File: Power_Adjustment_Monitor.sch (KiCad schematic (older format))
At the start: 15 parts

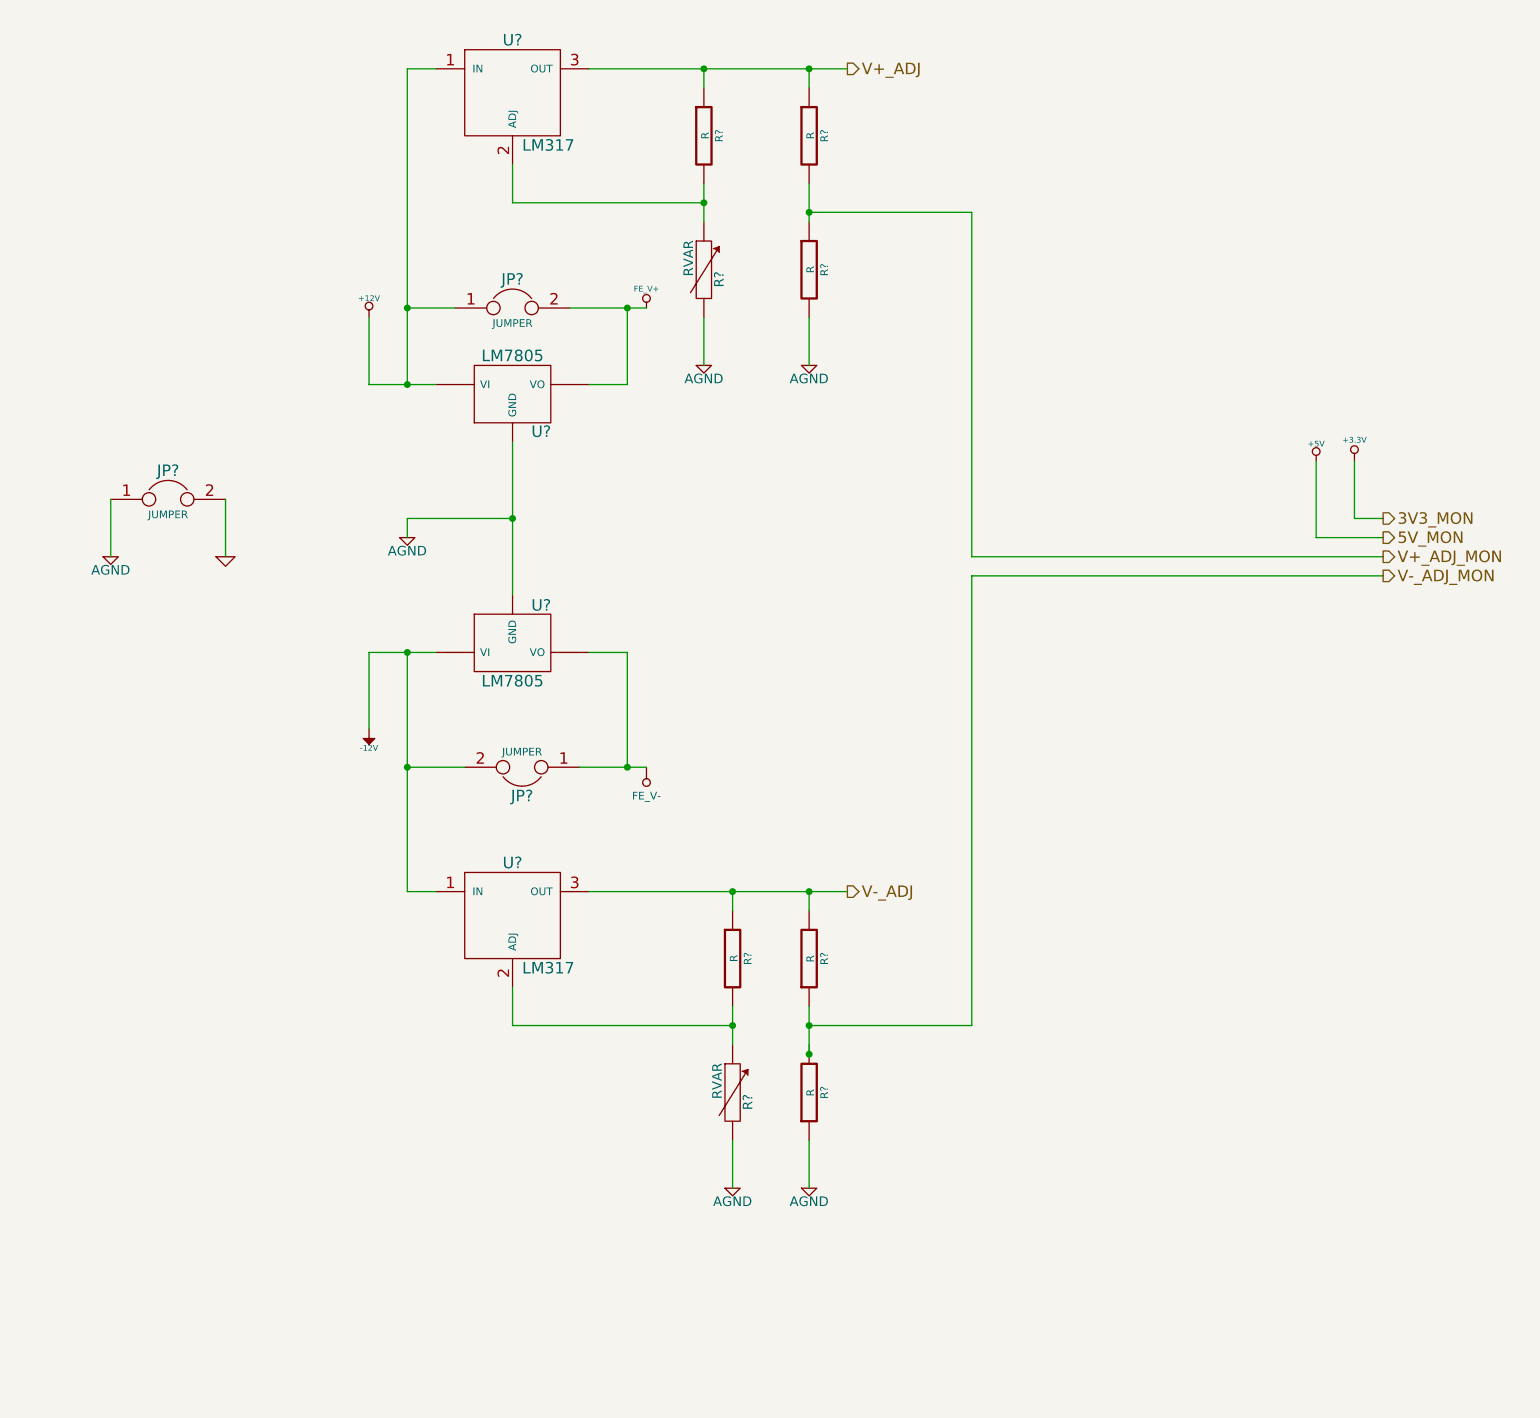
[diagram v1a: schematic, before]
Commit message: RELAY 02-20-2014
1) Created and associated footprints for relay module
2) Placed relay module's components in PCB layout
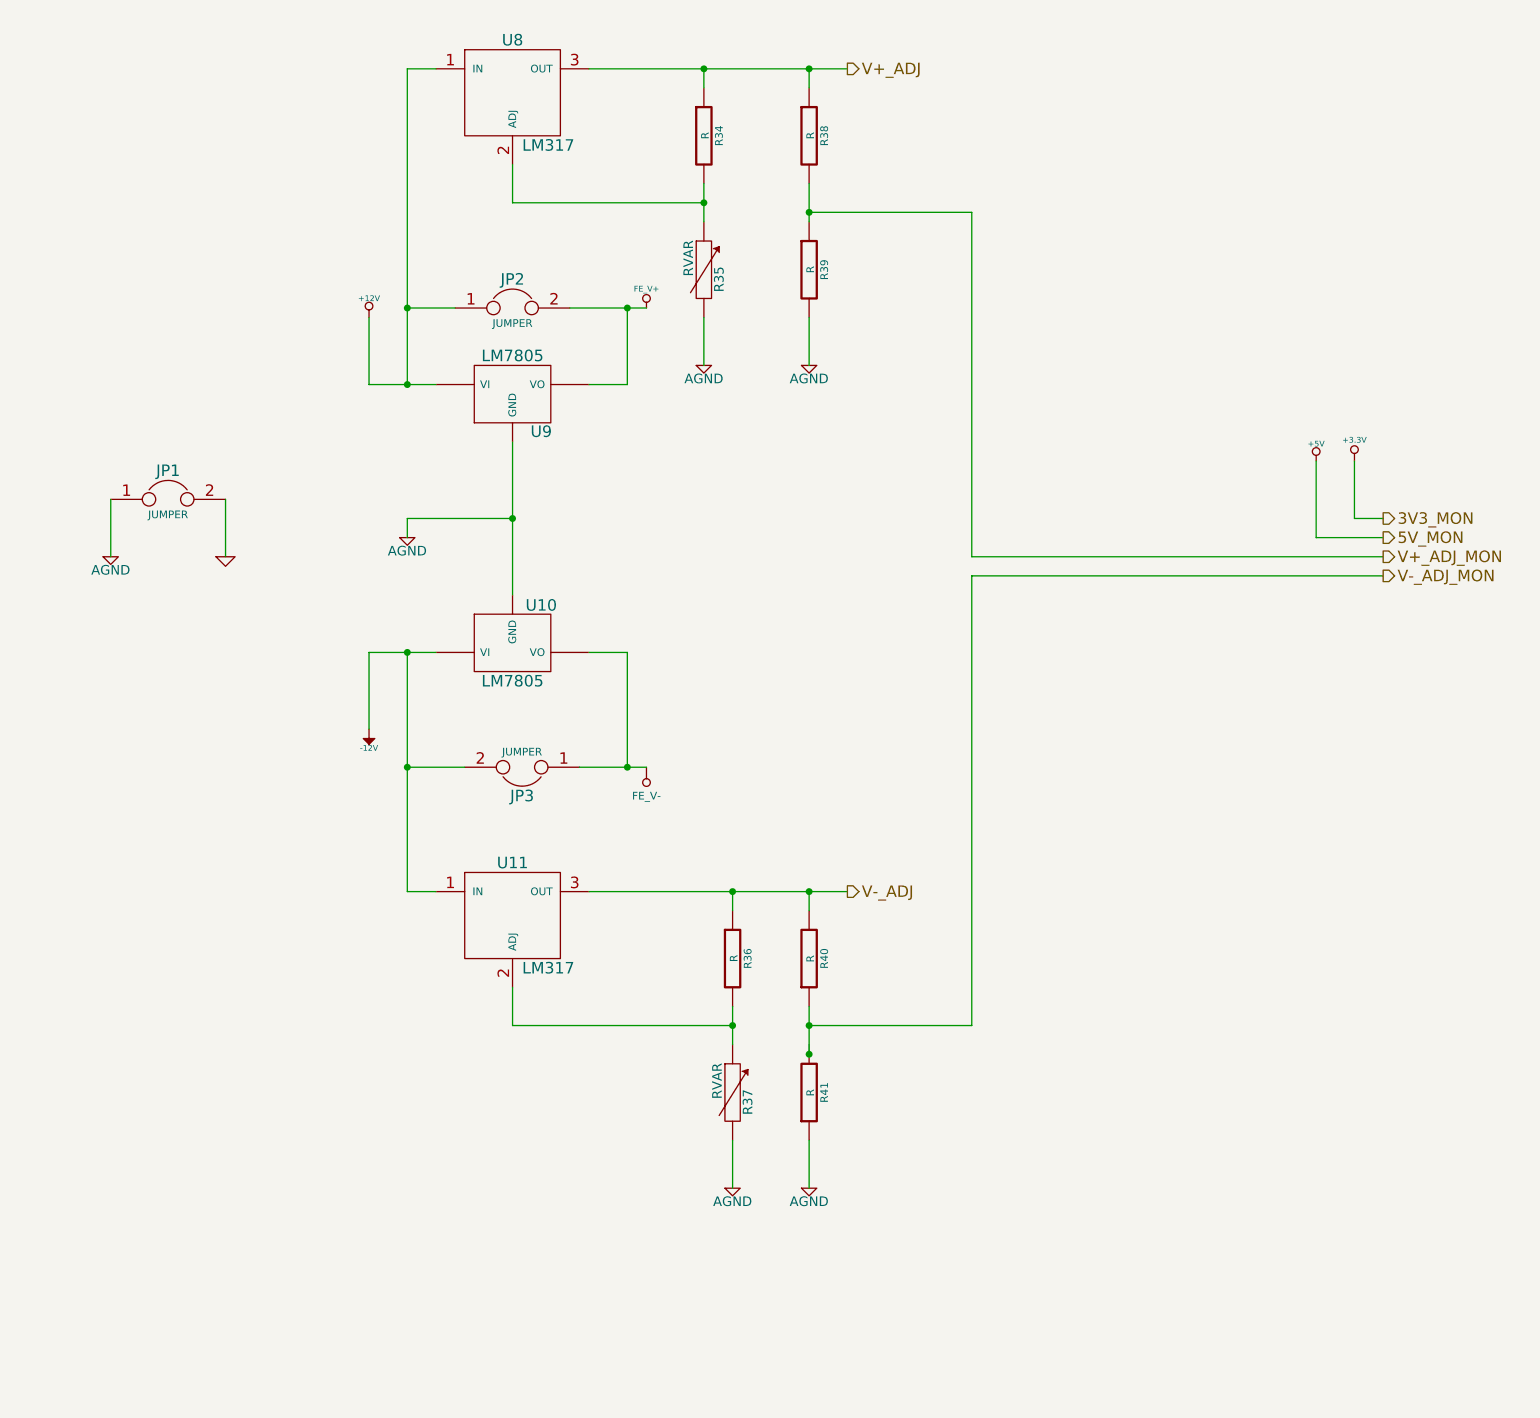
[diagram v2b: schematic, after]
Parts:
- gave numbers to parts that had none: 15
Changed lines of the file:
@@
 $Descr A4 11693 8268
 encoding utf-8
-Sheet 9 9
+Sheet 8 9
 Title ""
-Date "11 feb 2014"
+Date "20 feb 2014"
 Rev ""
 Comp ""
@@
 $EndDescr
 $Comp
-L +3.3V #PWR?
+L +3.3V #PWR57
 U 1 1 52F8235F
 P 8000 2850
-F 0 "#PWR?" H 8000 2810 30  0001 C CNN
+F 0 "#PWR57" H 8000 2810 30  0001 C CNN
 F 1 "+3.3V" H 8000 2960 30  0000 C CNN
 F 2 "" H 8000 2850 60  0000 C CNN
@@
 $EndComp
 $Comp
-L +5V #PWR?
+L +5V #PWR56
 U 1 1 52F82365
 P 7800 2850
-F 0 "#PWR?" H 7800 2940 20  0001 C CNN
+F 0 "#PWR56" H 7800 2940 20  0001 C CNN
 F 1 "+5V" H 7800 2940 30  0000 C CNN
 F 2 "" H 7800 2850 60  0000 C CNN
@@
 $EndComp
 $Comp
-L -12V #PWR?
+L -12V #PWR48
 U 1 1 52F823F0
 P 2850 4250
-F 0 "#PWR?" H 2850 4380 20  0001 C CNN
+F 0 "#PWR48" H 2850 4380 20  0001 C CNN
 F 1 "-12V" H 2850 4350 30  0000 C CNN
 F 2 "" H 2850 4250 60  0000 C CNN
@@
 $EndComp
 $Comp
-L +12V #PWR?
+L +12V #PWR47
 U 1 1 52F823F6
 P 2850 2100
-F 0 "#PWR?" H 2850 2050 20  0001 C CNN
+F 0 "#PWR47" H 2850 2050 20  0001 C CNN
 F 1 "+12V" H 2850 2200 30  0000 C CNN
 F 2 "" H 2850 2100 60  0000 C CNN
@@
 $EndComp
 $Comp
-L LM317 U?
+L LM317 U8
 U 1 1 52F82C8E
 P 3600 950
-F 0 "U?" H 3600 1250 60  0000 C CNN
+F 0 "U8" H 3600 1250 60  0000 C CNN
 F 1 "LM317" H 3650 700 60  0000 L CNN
 F 2 "~" H 3600 950 60  0000 C CNN
@@
 $EndComp
 $Comp
-L LM317 U?
+L LM317 U11
 U 1 1 52F82C9B
 P 3600 5250
-F 0 "U?" H 3600 5550 60  0000 C CNN
+F 0 "U11" H 3600 5550 60  0000 C CNN
 F 1 "LM317" H 3650 5000 60  0000 L CNN
 F 2 "~" H 3600 5250 60  0000 C CNN
@@
 $EndComp
 $Comp
-L JUMPER JP?
+L JUMPER JP2
 U 1 1 52F82CA3
 P 3600 2050
-F 0 "JP?" H 3600 2200 60  0000 C CNN
+F 0 "JP2" H 3600 2200 60  0000 C CNN
 F 1 "JUMPER" H 3600 1970 40  0000 C CNN
 F 2 "~" H 3600 2050 60  0000 C CNN
@@
 $EndComp
 $Comp
-L JUMPER JP?
+L JUMPER JP3
 U 1 1 52F82CFF
 P 3650 4450
-F 0 "JP?" H 3650 4600 60  0000 C CNN
+F 0 "JP3" H 3650 4600 60  0000 C CNN
 F 1 "JUMPER" H 3650 4370 40  0000 C CNN
 F 2 "~" H 3650 4450 60  0000 C CNN
@@
 $EndComp
 $Comp
-L AGND #PWR?
+L AGND #PWR49
 U 1 1 52F82FD1
 P 3050 3250
-F 0 "#PWR?" H 3050 3250 40  0001 C CNN
+F 0 "#PWR49" H 3050 3250 40  0001 C CNN
 F 1 "AGND" H 3050 3180 50  0000 C CNN
 F 2 "" H 3050 3250 60  0000 C CNN
@@
 $EndComp
 $Comp
-L AGND #PWR?
+L AGND #PWR45
 U 1 1 52F82FDE
 P 1500 3350
-F 0 "#PWR?" H 1500 3350 40  0001 C CNN
+F 0 "#PWR45" H 1500 3350 40  0001 C CNN
 F 1 "AGND" H 1500 3280 50  0000 C CNN
 F 2 "" H 1500 3350 60  0000 C CNN
@@
 $EndComp
 $Comp
-L GND #PWR?
+L GND #PWR46
 U 1 1 52F82FE6
 P 2100 3350
-F 0 "#PWR?" H 2100 3350 30  0001 C CNN
+F 0 "#PWR46" H 2100 3350 30  0001 C CNN
 F 1 "GND" H 2100 3280 30  0001 C CNN
 F 2 "" H 2100 3350 60  0000 C CNN
@@
 $EndComp
 $Comp
-L JUMPER JP?
+L JUMPER JP1
 U 1 1 52F82FF3
 P 1800 3050
-F 0 "JP?" H 1800 3200 60  0000 C CNN
+F 0 "JP1" H 1800 3200 60  0000 C CNN
 F 1 "JUMPER" H 1800 2970 40  0000 C CNN
 F 2 "~" H 1800 3050 60  0000 C CNN
@@
 $EndComp
 $Comp
-L FE_V+ #PWR?
+L FE_V+ #PWR50
 U 1 1 52F8326E
 P 4300 2050
-F 0 "#PWR?" H 4300 2150 30  0001 C CNN
+F 0 "#PWR50" H 4300 2150 30  0001 C CNN
 F 1 "FE_V+" H 4300 2150 30  0000 C CNN
 F 2 "" H 4300 2050 60  0000 C CNN
@@
 $EndComp
 $Comp
-L FE_V- #PWR?
+L FE_V- #PWR51
 U 1 1 52F83296
 P 4300 4450
-F 0 "#PWR?" H 4300 4650 40  0001 C CNN
+F 0 "#PWR51" H 4300 4650 40  0001 C CNN
 F 1 "FE_V-" H 4300 4600 40  0000 C CNN
 F 2 "" H 4300 4450 60  0000 C CNN
@@
 $EndComp
 $Comp
-L LM7805 U?
+L LM7805 U9
 U 1 1 52F832FF
 P 3600 2500
-F 0 "U?" H 3750 2304 60  0000 C CNN
+F 0 "U9" H 3750 2304 60  0000 C CNN
 F 1 "LM7805" H 3600 2700 60  0000 C CNN
 F 2 "~" H 3600 2500 60  0000 C CNN
@@
 $EndComp
 $Comp
-L LM7805 U?
+L LM7805 U10
 U 1 1 52F8330C
 P 3600 3800
-F 0 "U?" H 3750 3604 60  0000 C CNN
+F 0 "U10" H 3750 3604 60  0000 C CNN
 F 1 "LM7805" H 3600 4000 60  0000 C CNN
 F 2 "~" H 3600 3800 60  0000 C CNN
@@
 $EndComp
 $Comp
-L R R?
+L R R36
 U 1 1 52F8339C
 P 4750 5450
-F 0 "R?" V 4830 5450 40  0000 C CNN
+F 0 "R36" V 4830 5450 40  0000 C CNN
 F 1 "R" V 4757 5451 40  0000 C CNN
 F 2 "~" V 4680 5450 30  0000 C CNN
@@
 $EndComp
 $Comp
-L AGND #PWR?
+L AGND #PWR53
 U 1 1 52F8341A
 P 4750 6650
-F 0 "#PWR?" H 4750 6650 40  0001 C CNN
+F 0 "#PWR53" H 4750 6650 40  0001 C CNN
 F 1 "AGND" H 4750 6580 50  0000 C CNN
 F 2 "" H 4750 6650 60  0000 C CNN
@@
 $EndComp
 $Comp
-L R R?
+L R R34
 U 1 1 52F83471
 P 4600 1150
-F 0 "R?" V 4680 1150 40  0000 C CNN
+F 0 "R34" V 4680 1150 40  0000 C CNN
 F 1 "R" V 4607 1151 40  0000 C CNN
 F 2 "~" V 4530 1150 30  0000 C CNN
@@
 $EndComp
 $Comp
-L AGND #PWR?
+L AGND #PWR52
 U 1 1 52F83482
 P 4600 2350
-F 0 "#PWR?" H 4600 2350 40  0001 C CNN
+F 0 "#PWR52" H 4600 2350 40  0001 C CNN
 F 1 "AGND" H 4600 2280 50  0000 C CNN
 F 2 "" H 4600 2350 60  0000 C CNN
@@
 V-_ADJ_MON
 $Comp
-L RVAR R?
+L RVAR R37
 U 1 1 52F8361B
 P 4750 6150
-F 0 "R?" V 4830 6100 50  0000 C CNN
+F 0 "R37" V 4830 6100 50  0000 C CNN
 F 1 "RVAR" V 4670 6210 50  0000 C CNN
 F 2 "~" H 4750 6150 60  0000 C CNN
@@
 $EndComp
 $Comp
-L RVAR R?
+L RVAR R35
 U 1 1 52F8362A
 P 4600 1850
-F 0 "R?" V 4680 1800 50  0000 C CNN
+F 0 "R35" V 4680 1800 50  0000 C CNN
 F 1 "RVAR" V 4520 1910 50  0000 C CNN
 F 2 "~" H 4600 1850 60  0000 C CNN
@@
 $EndComp
 $Comp
-L R R?
+L R R38
 U 1 1 52F83637
 P 5150 1150
-F 0 "R?" V 5230 1150 40  0000 C CNN
+F 0 "R38" V 5230 1150 40  0000 C CNN
 F 1 "R" V 5157 1151 40  0000 C CNN
 F 2 "~" V 5080 1150 30  0000 C CNN
@@
 $EndComp
 $Comp
-L R R?
+L R R39
 U 1 1 52F8363D
 P 5150 1850
-F 0 "R?" V 5230 1850 40  0000 C CNN
+F 0 "R39" V 5230 1850 40  0000 C CNN
 F 1 "R" V 5157 1851 40  0000 C CNN
 F 2 "~" V 5080 1850 30  0000 C CNN
@@
 $EndComp
 $Comp
-L R R?
+L R R41
 U 1 1 52F836E6
 P 5150 6150
-F 0 "R?" V 5230 6150 40  0000 C CNN
+F 0 "R41" V 5230 6150 40  0000 C CNN
 F 1 "R" V 5157 6151 40  0000 C CNN
 F 2 "~" V 5080 6150 30  0000 C CNN
@@
 $EndComp
 $Comp
-L R R?
+L R R40
 U 1 1 52F836EC
 P 5150 5450
-F 0 "R?" V 5230 5450 40  0000 C CNN
+F 0 "R40" V 5230 5450 40  0000 C CNN
 F 1 "R" V 5157 5451 40  0000 C CNN
 F 2 "~" V 5080 5450 30  0000 C CNN
@@
 $EndComp
 $Comp
-L AGND #PWR?
+L AGND #PWR54
 U 1 1 52F8382B
 P 5150 2350
-F 0 "#PWR?" H 5150 2350 40  0001 C CNN
+F 0 "#PWR54" H 5150 2350 40  0001 C CNN
 F 1 "AGND" H 5150 2280 50  0000 C CNN
 F 2 "" H 5150 2350 60  0000 C CNN
@@
 $EndComp
 $Comp
-L AGND #PWR?
+L AGND #PWR55
 U 1 1 52F83839
 P 5150 6650
-F 0 "#PWR?" H 5150 6650 40  0001 C CNN
+F 0 "#PWR55" H 5150 6650 40  0001 C CNN
 F 1 "AGND" H 5150 6580 50  0000 C CNN
 F 2 "" H 5150 6650 60  0000 C CNN
